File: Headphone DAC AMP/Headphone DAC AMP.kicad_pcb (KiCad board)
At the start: 4 copper layers, 56.4 x 97.2 mm, 165 parts, among them J1 2137160001, J2 M50-3551042, J3 SJ-3502-SMT, J4 PINHD_1x2_Male, J5 PINHD_2x3_Male, U1 ES9039Q2M, U11 ADP5071AREZ-R7, U12 TPS74501PDRVR, U14 ADP7185ACPZN-R7, U2 XU316-1024-QF60B-C24, U3 TPA6120A2DWP, U4 OPA1612AxD, U5 OPA1612AxD, U6 MCP1727-1802xSN, U7 MCP1727-3302xSN, U8 W25Q16JVSNIQ, U9 TPS717XX, Y1 Crystal_GND24, Y2 LMK6CE049152CDLFR, Y3 ASDLJ-E-45.1584MHz

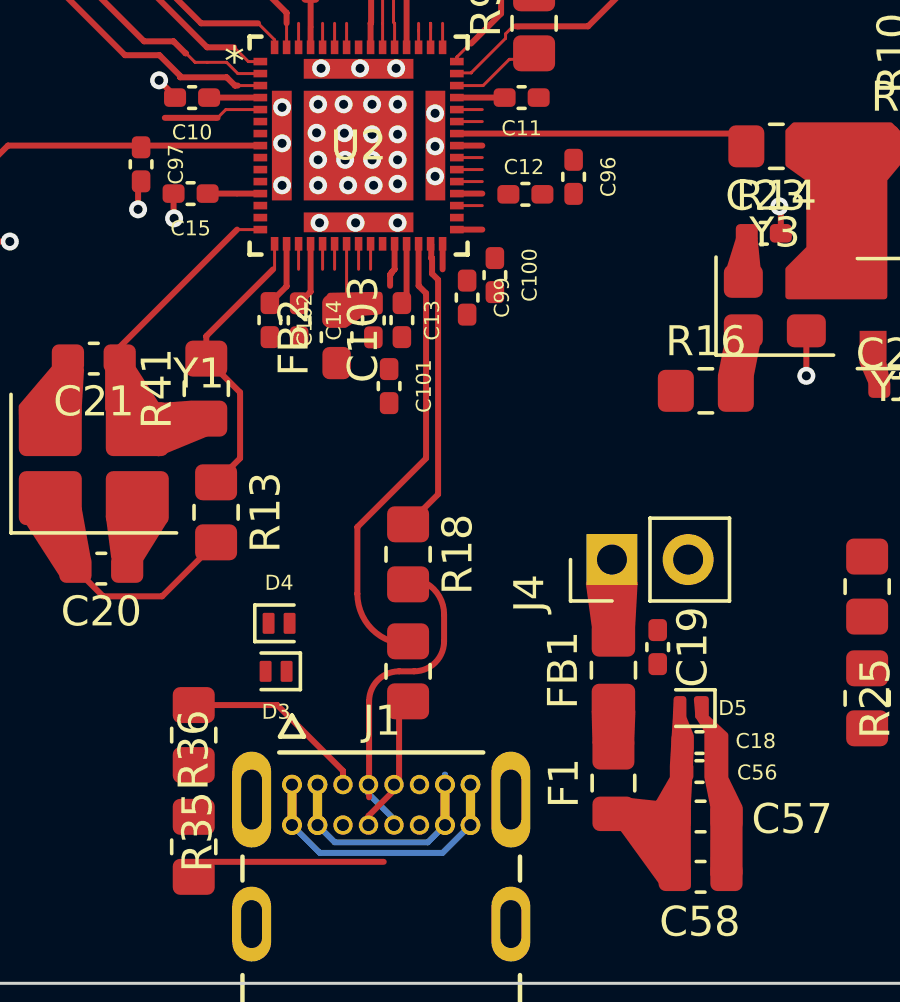
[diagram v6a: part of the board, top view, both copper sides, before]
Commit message: holy fuck all that work for the width to pe .1mm for an impedance of 85ohm
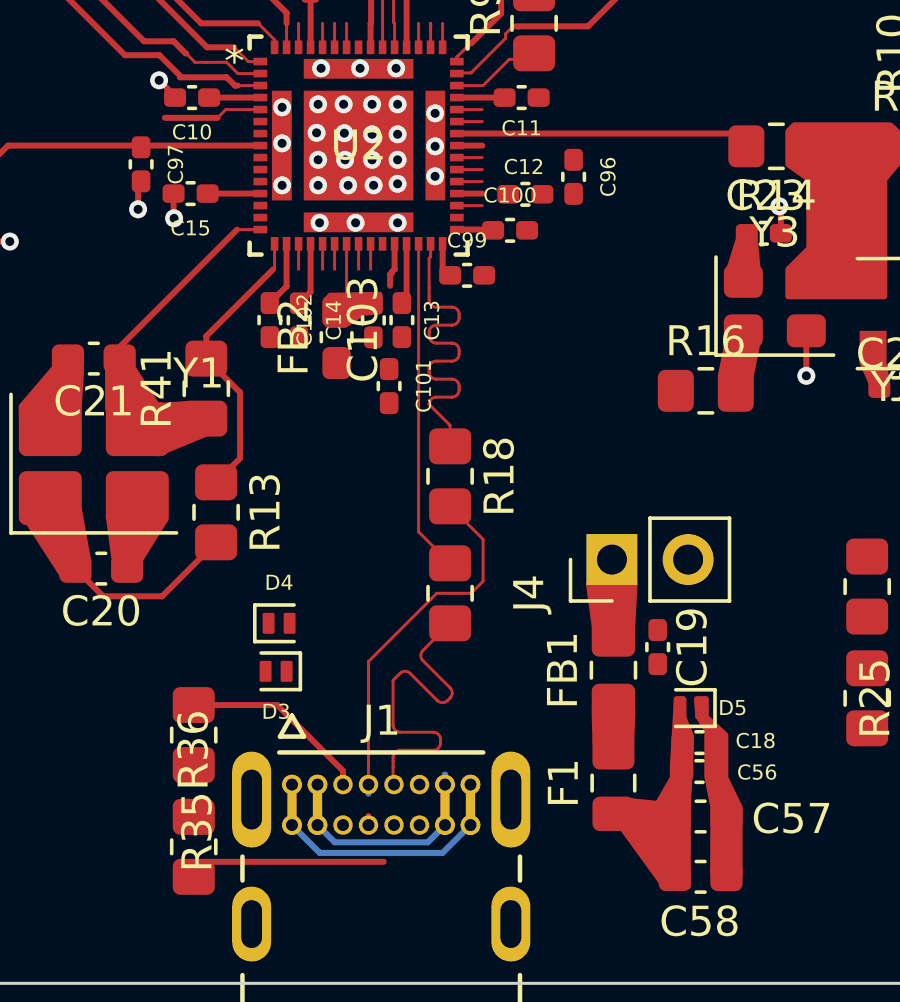
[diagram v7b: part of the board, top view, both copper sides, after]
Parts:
- moved R18 2.95 mm to (100.1, 133.0)
- moved R19 2.95 mm to (100.1, 136.9)
- moved C100 1.58 mm to (102.1, 124.8), turned to 0 degrees
- moved C99 0.74 mm to (100.7, 126.3), turned to 0 degrees
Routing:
- net /USB Audio Input/PRED+: track 1.70 -> 12.5 mm
- net /USB Audio Input/PRED-: track 4.67 -> 12.7 mm
- net /USB Audio Input/D+: track 9.88 -> 11.7 mm
- net /USB Audio Input/D-: track 12.7 -> 11.1 mm

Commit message: Routed micilanious traces and finished D +-
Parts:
- moved D3 12.4 mm to (100.8, 128.9)
- moved D4 5.27 mm to (98.1, 134.1)
- moved C96 1.16 mm to (105.2, 122.4)
- moved C12 0.98 mm to (103.3, 122.9)
- moved C16 0.14 mm to (99.5, 116.6)
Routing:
- net /Clocking/XTAL1_EN: track 0.80 -> 34.3 mm, vias 0 -> 2
- net /DAC/SDA: track 1.84 -> 22.9 mm, vias 1 -> 2
- net /DAC/SCL: track 2.23 -> 20.4 mm, vias 1 -> 2
- net /Audio Rails/-5V5: track 0.00 -> 16.8 mm
- net /DAC/EN: track 0.80 -> 14.6 mm, vias 0 -> 2
- net Net-(U11-COMP1): track 0.00 -> 8.12 mm
- net Net-(U11-FB2): track 0.00 -> 6.47 mm
- net Net-(U11-COMP2): track 0.00 -> 6.46 mm
- net /Audio Rails/+5V5: track 2.57 -> 8.98 mm
- net /Audio Rails/5Vin: track 0.00 -> 6.07 mm
- net Net-(U11-SS): track 0.00 -> 5.14 mm, vias 0 -> 2
- net Net-(U11-FB1): track 0.00 -> 4.35 mm
- net /Audio Rails/VREF: track 0.00 -> 3.68 mm
- net /Debug/4D0: track 0.85 -> 2.95 mm, vias 0 -> 1
- net 0V9: track 13.6 -> 15.5 mm
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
